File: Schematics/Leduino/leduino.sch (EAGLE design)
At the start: 31 parts, among them J1 POWER_JACKCOMBO

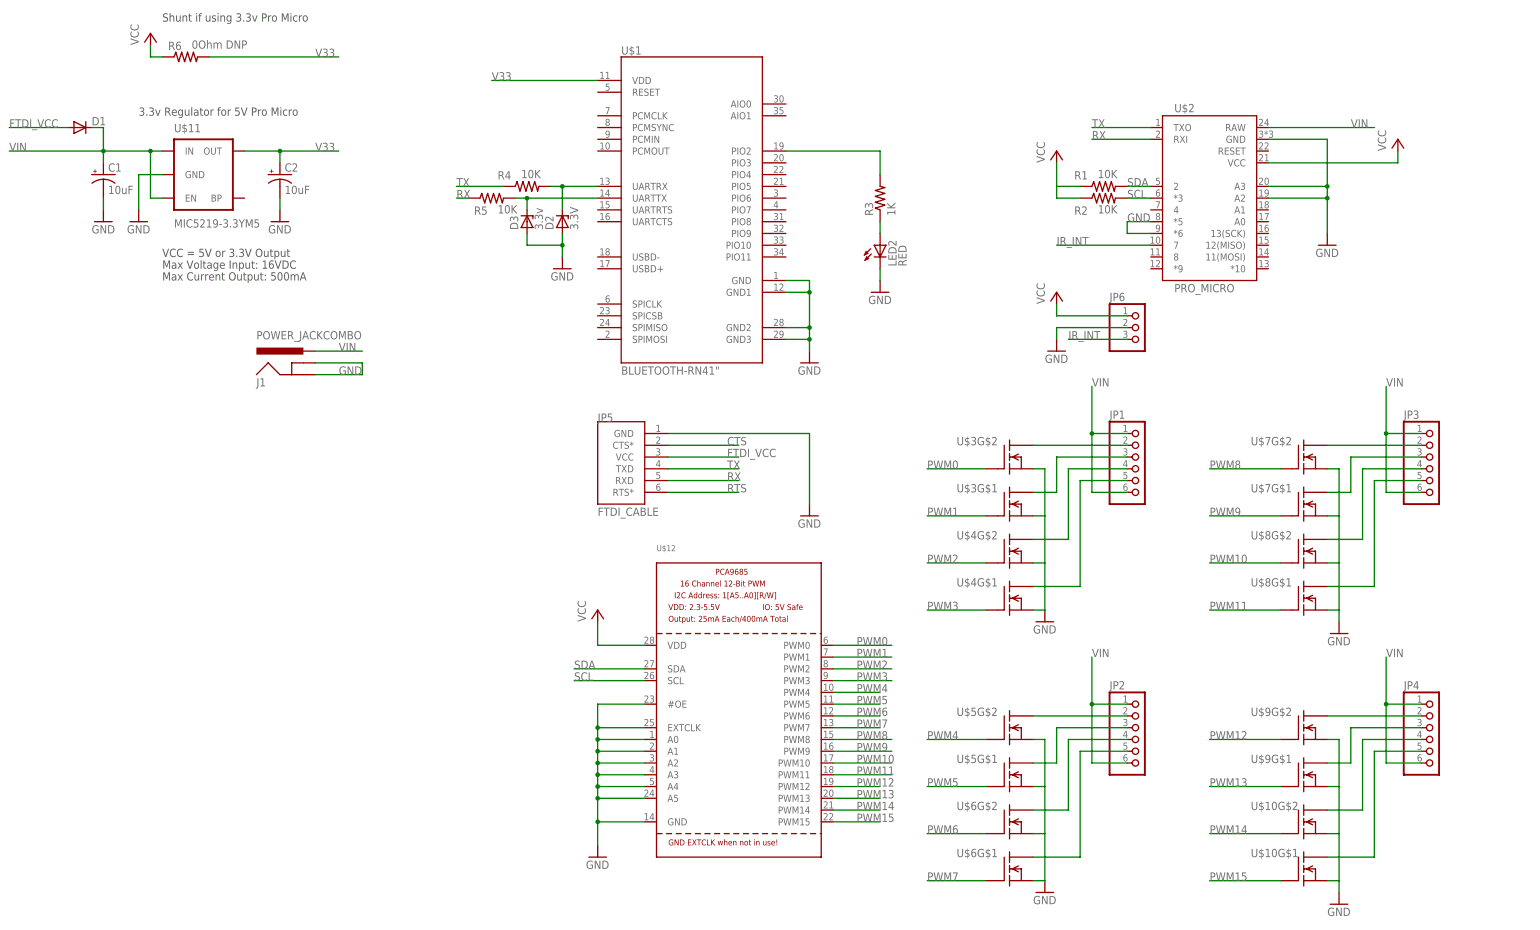
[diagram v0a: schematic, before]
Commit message: Making progress, attempting to hack the autorouter
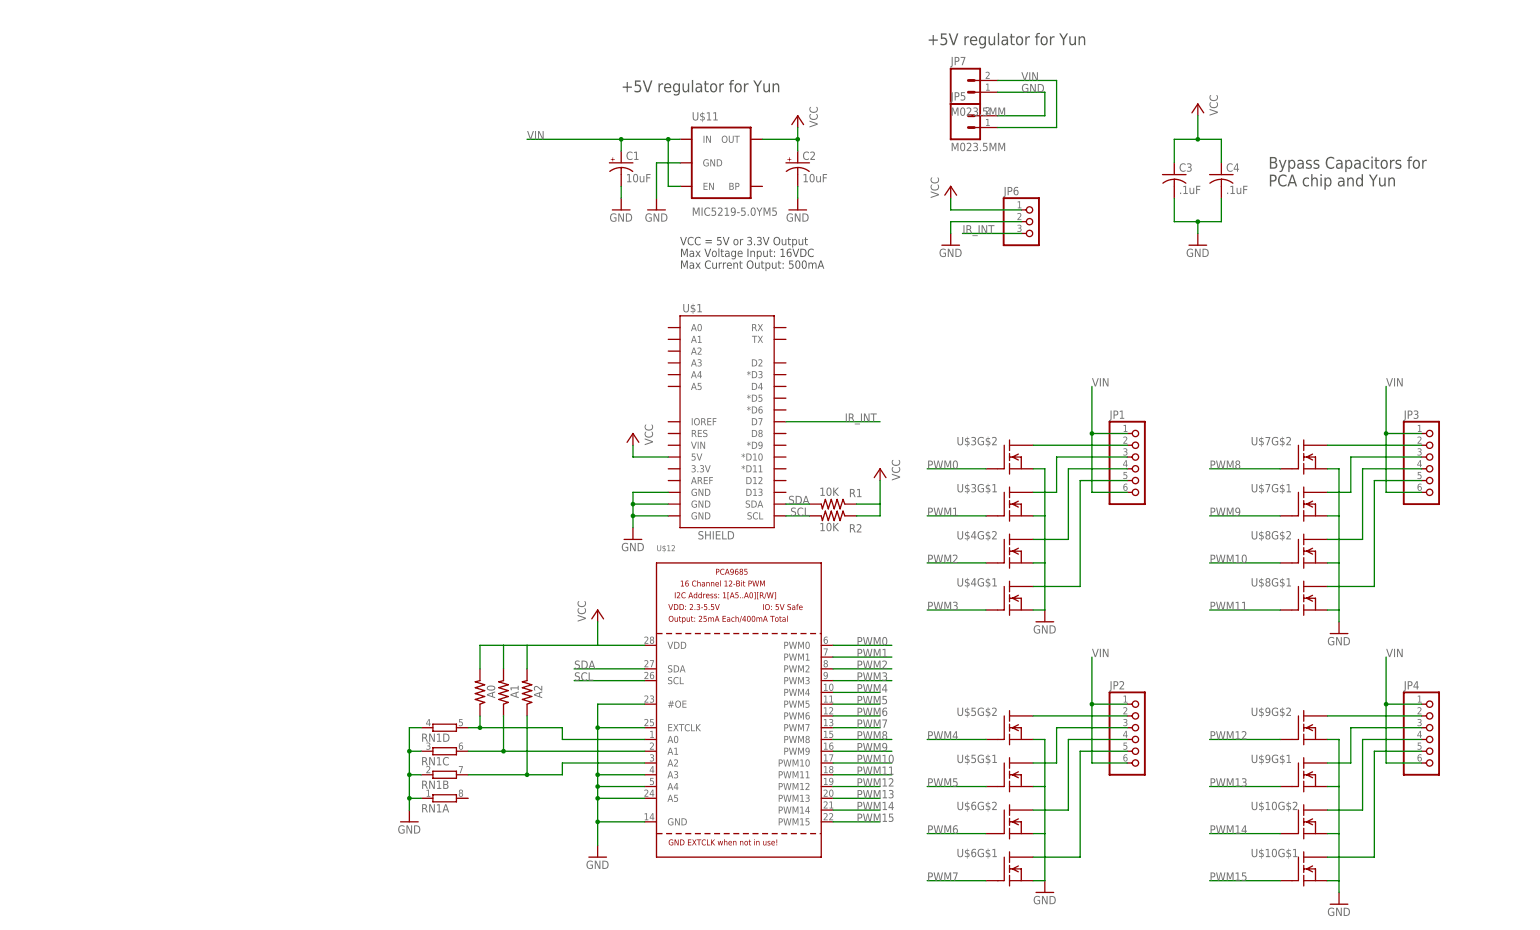
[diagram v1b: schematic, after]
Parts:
- removed D1: (no value), SparkFun:DIODESOD
- removed D2: 3.3V, diode:ZENER-DIODESOD80C
- removed D3: 3.3v, diode:ZENER-DIODESOD80C
- removed J1: POWER_JACKCOMBO, SparkFun-Connectors:POWER_JACKCOMBO
- removed LED2: RED, led:LEDSML0805
- removed R3: 1K, rcl:R-US_R0805
- removed R4, R5: 10K, rcl:R-US_R0805
- removed R6: 0Ohm DNP, rcl:R-US_R0805
- removed U$2: PRO_MICRO, Leduino:ARDUINO_PRO_MICRO_SMD
- added A0, A1, A2: 0 Ohm DNP, rcl:R-US_R0805
- added C3, C4: .1uF, rcl:C-USC0805
- added JP7: M023.5MM, SparkFun-Connectors:M023.5MM
- added RN1: (no value), resistor-dil:4R-NEXB38V
- JP5: value FTDI_CABLE -> M023.5MM; device Leduino:FTDI_CABLE -> SparkFun-Connectors:M023.5MM
- U$1: value BLUETOOTH-RN41" -> SHIELD; device Leduino:BLUETOOTH-RN41" -> Leduino:ARDUINO_R3_SHIELD
- U$11: value MIC5219-3.3YM5 -> MIC5219-5.0YM5
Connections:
- removed net CTS: JP5.CTS*
- removed net FTDI_VCC: D1.A, JP5.VCC
- removed net N$13: R3.2, U$1.PIO2
- removed net N$14: D2.C, R4.2, U$1.UARTRX
- removed net N$38: LED2.A, R3.1
- removed net RTS: JP5.RTS*
- removed net RX: JP5.RXD, R5.1, U$2.RXI
- removed net TX: JP5.TXD, R4.1, U$2.TXO
- removed net V33: C2.+, R6.2, U$1.VDD, U$11.OUT
- new net N$16: A1.1, RN1C.2, U$12.A1
- new net N$21: A2.1, RN1B.2, U$12.A2
- net GND: now also C3.2, C4.2, JP5.2, JP7.1, RN1A.1, RN1B.1, RN1C.1, RN1D.1, U$1.GND@0, U$1.GND@1, U$1.GND@2; no longer D2.A, D3.A, J1.GND, J1.GNDBREAK, JP5.GND, LED2.C, U$1.GND, U$1.GND1, U$1.GND2, U$1.GND3, U$12.A0, U$12.A1, U$12.A2, U$2.*5, U$2.*6, U$2.A2, U$2.A3, U$2.GND
- net IR_INT: now also U$1.D7; no longer U$2.7
- net N$15: now also A0.1, RN1D.2, U$12.A0; no longer D3.C, R5.2, U$1.UARTTX
- net SCL: now also U$1.SCL; no longer U$2.*3
- net SDA: now also U$1.SDA; no longer U$2.2
- net VCC: now also A0.2, A1.2, A2.2, C2.+, C3.1, C4.1, U$1.5V, U$11.OUT; no longer R6.1, U$2.VCC
- net VIN: now also JP5.1, JP7.2; no longer D1.C, J1.PWR, U$2.RAW
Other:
- note added: "+5V regulator for Yun"
- note added: "Bypass Capacitors for PCA chip and Yun"
- note removed: "3.3v Regulator for 5V Pro Micro"
- note removed: "Shunt if using 3.3v Pro Micro"
- moved on the sheet: C1, C2, JP6, R1, R2, U$11

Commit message: Finished Layout, cleared DRC
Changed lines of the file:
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@@
 <part name="JP3" library="Leduino" deviceset="PINHD-1X6" device="3.5MM-RA"/>
 <part name="JP4" library="Leduino" deviceset="PINHD-1X6" device="3.5MM-RA"/>
-<part name="U$3" library="Leduino" deviceset="DMN6040SSD" device="" value=""/>
-<part name="U$4" library="Leduino" deviceset="DMN6040SSD" device="" value=""/>
-<part name="U$5" library="Leduino" deviceset="DMN6040SSD" device="" value=""/>
-<part name="U$6" library="Leduino" deviceset="DMN6040SSD" device="" value=""/>
-<part name="U$7" library="Leduino" deviceset="DMN6040SSD" device="" value=""/>
-<part name="U$8" library="Leduino" deviceset="DMN6040SSD" device="" value=""/>
-<part name="U$9" library="Leduino" deviceset="DMN6040SSD" device="" value=""/>
-<part name="U$10" library="Leduino" deviceset="DMN6040SSD" device="" value=""/>
+<part name="U$3" library="Leduino" deviceset="DMN6040SSD" device="" value="DMN6040SSD"/>
+<part name="U$4" library="Leduino" deviceset="DMN6040SSD" device="" value="DMN6040SSD"/>
+<part name="U$5" library="Leduino" deviceset="DMN6040SSD" device="" value="DMN6040SSD"/>
+<part name="U$6" library="Leduino" deviceset="DMN6040SSD" device="" value="DMN6040SSD"/>
+<part name="U$7" library="Leduino" deviceset="DMN6040SSD" device="" value="DMN6040SSD"/>
+<part name="U$8" library="Leduino" deviceset="DMN6040SSD" device="" value="DMN6040SSD"/>
+<part name="U$9" library="Leduino" deviceset="DMN6040SSD" device="" value="DMN6040SSD"/>
+<part name="U$10" library="Leduino" deviceset="DMN6040SSD" device="" value="DMN6040SSD"/>
 <part name="C2" library="SparkFun" deviceset="CAP_POL" device="1206" value="10uF"/>
 <part name="GND25" library="SparkFun" deviceset="GND" device=""/>
@@
 <pinref part="U$4" gate="G$1" pin="S"/>
 <pinref part="U$4" gate="G$2" pin="S"/>
+<junction x="96.52" y="-25.4"/>
+<junction x="96.52" y="-15.24"/>
+<junction x="96.52" y="-5.08"/>
 </segment>
 <segment>
@@
 <pinref part="U$6" gate="G$1" pin="S"/>
 <pinref part="U$6" gate="G$2" pin="S"/>
+<junction x="96.52" y="-83.82"/>
+<junction x="96.52" y="-73.66"/>
+<junction x="96.52" y="-63.5"/>
 </segment>
 <segment>
@@
 <pinref part="U$8" gate="G$1" pin="S"/>
 <pinref part="U$8" gate="G$2" pin="S"/>
+<junction x="160.02" y="-5.08"/>
+<junction x="160.02" y="-15.24"/>
+<junction x="160.02" y="-25.4"/>
 </segment>
 <segment>
@@
 <pinref part="U$10" gate="G$1" pin="S"/>
 <pinref part="U$10" gate="G$2" pin="S"/>
+<junction x="160.02" y="-83.82"/>
+<junction x="160.02" y="-73.66"/>
+<junction x="160.02" y="-63.5"/>
 </segment>
 <segment>
@@
 <pinref part="R1" gate="G$1" pin="1"/>
 <wire x1="55.88" y1="-2.54" x2="60.96" y2="-2.54" width="0.1524" layer="91"/>
+<junction x="60.96" y="-2.54"/>
 </segment>
 <segment>
@@
 <pinref part="A2" gate="G$1" pin="2"/>
 <wire x1="-15.24" y1="-38.1" x2="-15.24" y2="-33.02" width="0.1524" layer="91"/>
+<junction x="-15.24" y="-33.02"/>
+<junction x="-20.32" y="-33.02"/>
+<junction x="0" y="-33.02"/>
 </segment>
 <segment>
@@
 </sheet>
 </sheets>
+<errors>
+</errors>
 </schematic>
 </drawing>

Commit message: Cleaned up silkscreen, passed freedDFM
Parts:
- JP1, JP2: value (none) -> M023.5MM; device Leduino:PINHD-1X63.5MM-RA -> SparkFun-Connectors:M023.5MM
- JP3: device Leduino:PINHD-1X63.5MM-RA -> adafruit:PINHD-1X3
- JP5, JP7: value M023.5MM -> (none); device SparkFun-Connectors:M023.5MM -> Leduino:PINHD-1X63.5MM-RA
- JP6: device adafruit:PINHD-1X3 -> Leduino:PINHD-1X63.5MM-RA
- renumbered U$1 to S1, U$10 to U10, U$11 to U1, U$12 to U2, U$3 to U3, U$4 to U4, U$5 to U5, U$6 to U6, U$7 to U7, U$8 to U8, U$9 to U9
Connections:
- net GND: now also JP1.1, JP2.2, JP3.2; no longer JP5.2, JP6.2, JP7.1
- net IR_INT: now also JP3.3; no longer JP6.3
- net N$1: now also JP4.2; no longer JP1.2
- net N$10: now also JP5.3; no longer JP2.3
- net N$11: now also JP5.5; no longer JP2.5
- net N$12: now also JP5.4; no longer JP2.4
- net N$17: now also JP6.2; no longer JP3.2
- net N$18: now also JP6.3; no longer JP3.3
- net N$19: now also JP6.5; no longer JP3.5
- net N$2: now also JP4.3; no longer JP1.3
- net N$20: now also JP6.4; no longer JP3.4
- net N$3: now also JP4.5; no longer JP1.5
- net N$4: now also JP4.4; no longer JP1.4
- net N$5: now also JP7.2; no longer JP4.2
- net N$6: now also JP7.3; no longer JP4.3
- net N$7: now also JP7.5; no longer JP4.5
- net N$8: now also JP7.4; no longer JP4.4
- net N$9: now also JP5.2; no longer JP2.2
- net VCC: now also JP3.1; no longer JP6.1
- net VIN: now also JP1.2, JP5.6, JP6.1, JP6.6, JP7.1, JP7.6; no longer JP1.1, JP1.6, JP2.6, JP3.1, JP3.6, JP7.2
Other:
- moved on the sheet: JP4

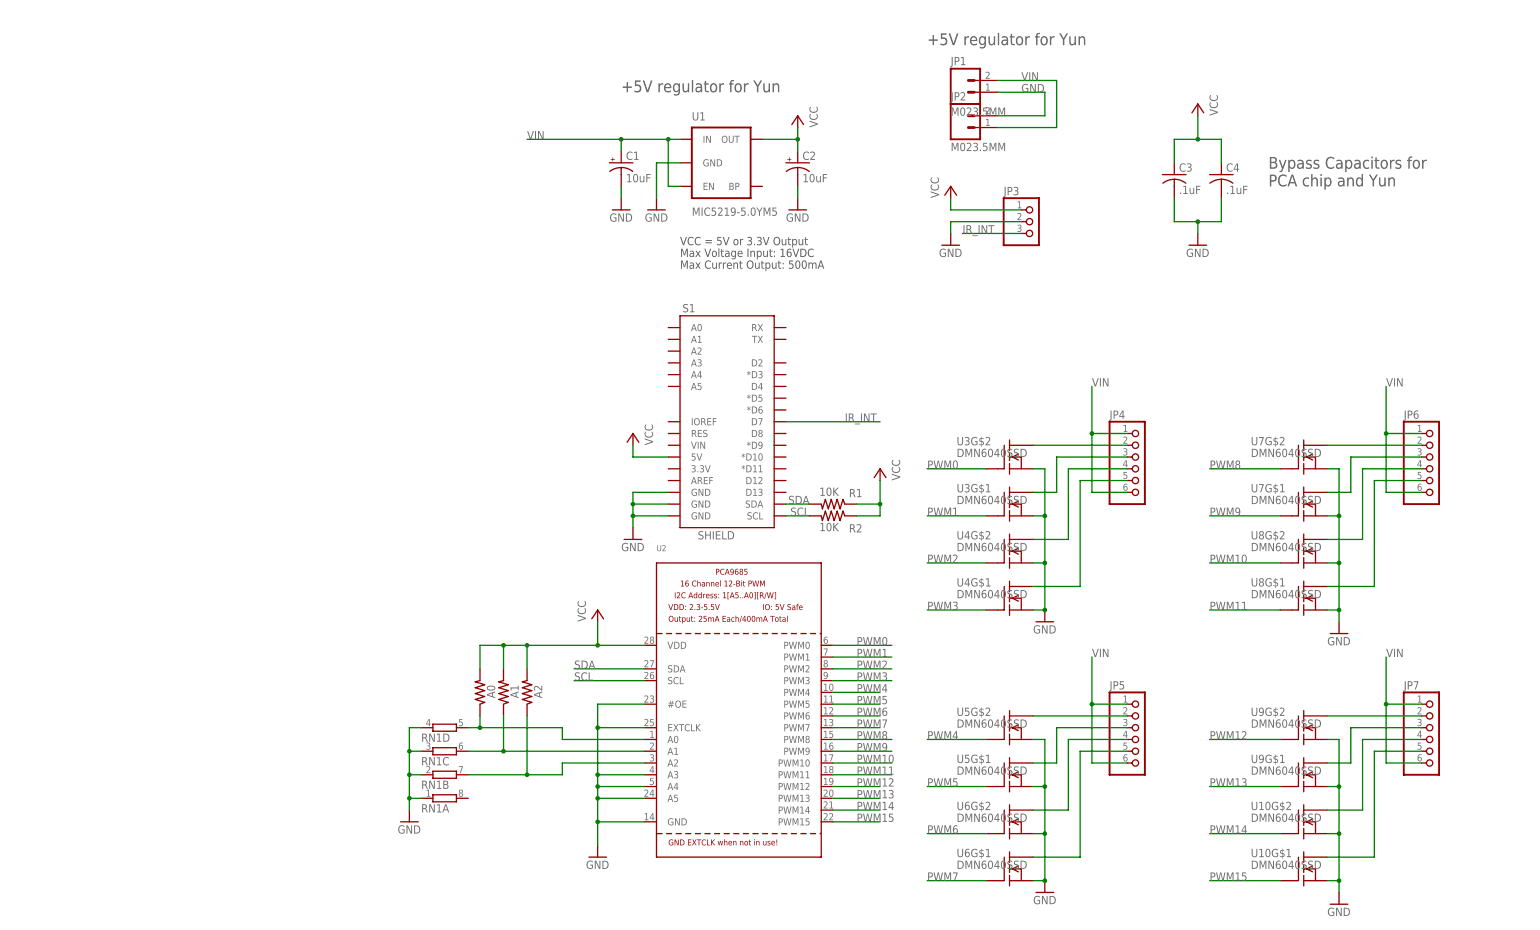
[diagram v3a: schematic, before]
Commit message: Designed and Laid out Board Rev 2.0 ready for review
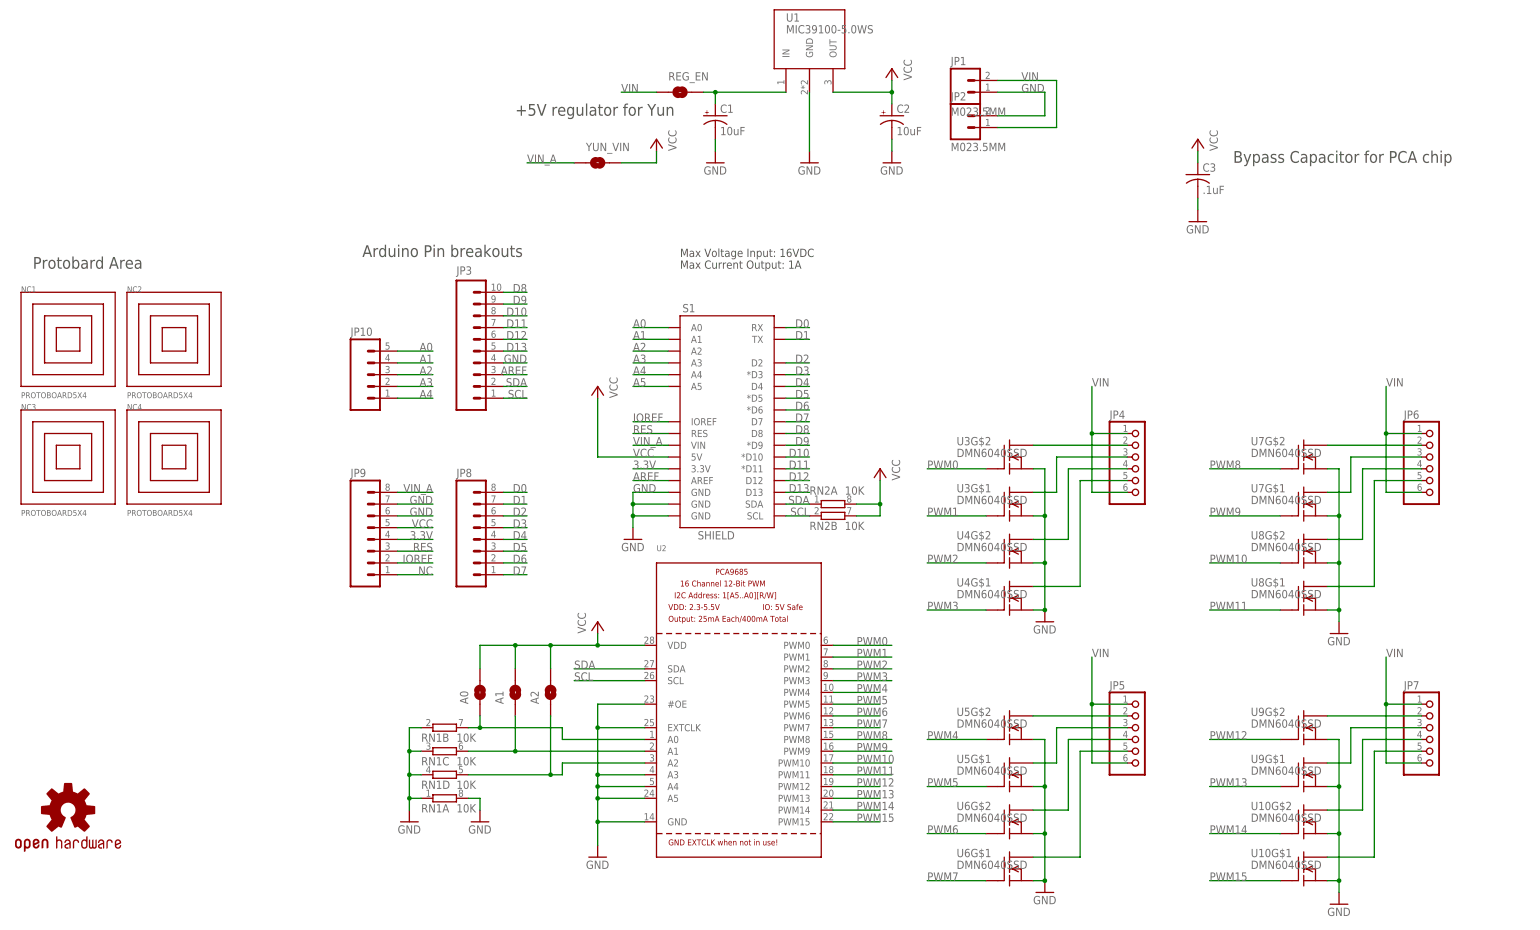
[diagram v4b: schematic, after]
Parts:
- removed C4: .1uF, rcl:C-USC0805
- removed R1, R2: 10K, rcl:R-US_R0805
- added JP10: (no value), SparkFun-Connectors:M05NO_SILK
- added JP8, JP9: (no value), SparkFun-Connectors:M08NO_SILK_FEMALE_PTH
- added NC1, NC2, NC3, NC4: PROTOBOARD5X4, Leduino:PROTOBOARD5X4
- added REG_EN, YUN_VIN: SOLDERJUMPERNO, Leduino:SOLDERJUMPERNO
- added RN2: 10K, resistor-dil:4R-NEXB38V
- added U$1: OSHW-LOGOL, Pro_Micro:OSHW-LOGOL
- A0, A1, A2: value 0 Ohm DNP -> SOLDERJUMPERNO; device rcl:R-US_R0805 -> Leduino:SOLDERJUMPERNO
- JP3: value (none) -> M10NO_SILK_PTH_FEMALE; device adafruit:PINHD-1X3 -> SparkFun-Connectors:M10NO_SILK_PTH_FEMALE
- RN1: value (none) -> 10K
- U1: value MIC5219-5.0YM5 -> MIC39100-5.0WS; device SparkFun:V_REG_LDOSMD -> Leduino:MIC39100
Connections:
- removed net IR_INT: JP3.3, S1.D7
- new net 3.3V: JP9.4, S1.3.3V
- new net A0: JP10.5, S1.A0
- new net A1: JP10.4, S1.A1
- new net A2: JP10.3, S1.A2
- new net A3: JP10.2, S1.A3
- new net A4: JP10.1, S1.A4
- new net A5: S1.A5
- new net AREF: JP3.3, S1.AREF
- new net D0: JP8.8, S1.RX
- new net D1: JP8.7, S1.TX
- new net D10: JP3.8, S1.*D10
- new net D11: JP3.7, S1.*D11
- new net D12: JP3.6, S1.D12
- new net D13: JP3.5, S1.D13
- new net D2: JP8.6, S1.D2
- new net D3: JP8.5, S1.*D3
- new net D4: JP8.4, S1.D4
- new net D5: JP8.3, S1.*D5
- new net D6: JP8.2, S1.*D6
- new net D7: JP8.1, S1.D7
- new net D8: JP3.10, S1.D8
- new net D9: JP3.9, S1.*D9
- new net IOREF: JP9.2, S1.IOREF
- new net N$13: C1.+, REG_EN.2, U1.IN
- new net NC: JP9.1
- new net RES: JP9.3, S1.RES
- new net VIN_A: JP9.8, S1.VIN, YUN_VIN.1
- net GND: now also JP3.4, JP9.6, JP9.7, RN1A.2; no longer C4.2, JP3.2
- net N$15: now also RN1B.2; no longer RN1D.2
- net N$21: now also RN1D.2; no longer RN1B.2
- net SCL: now also JP3.1, RN2B.1; no longer R2.2
- net SDA: now also JP3.2, RN2A.1; no longer R1.2
- net VCC: now also JP9.5, RN2A.2, RN2B.2, YUN_VIN.2; no longer C4.1, JP3.1, R1.1, R2.1
- net VIN: now also REG_EN.1; no longer C1.+, U1.EN, U1.IN
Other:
- note added: "Arduino Pin breakouts"
- note added: "Bypass Capacitor for PCA chip"
- note added: "Max Current Output: 1A"
- note added: "Protobard Area"
- note removed: "Bypass Capacitors for PCA chip and Yun"
- note removed: "Max Current Output: 500mA"
- note removed: "VCC = 5V or 3.3V Output"
- moved on the sheet: C1, C2, C3, RN1B, RN1D
